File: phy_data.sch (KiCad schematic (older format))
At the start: 18 parts

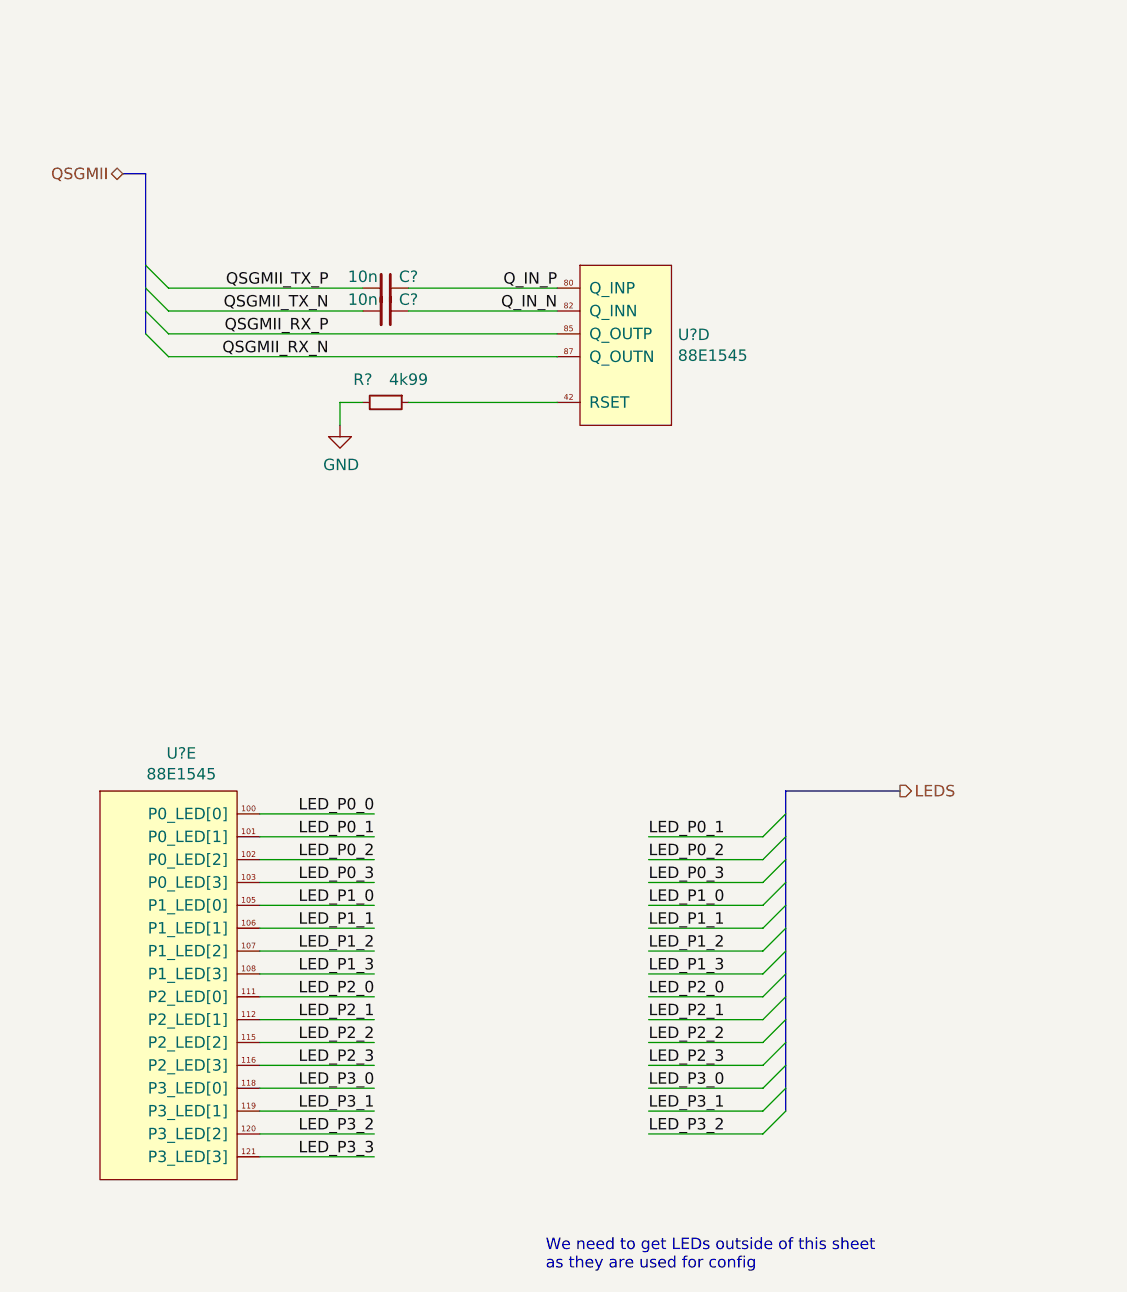
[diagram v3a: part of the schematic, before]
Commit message: sch: Remove ALL busses since kicad's support is broken
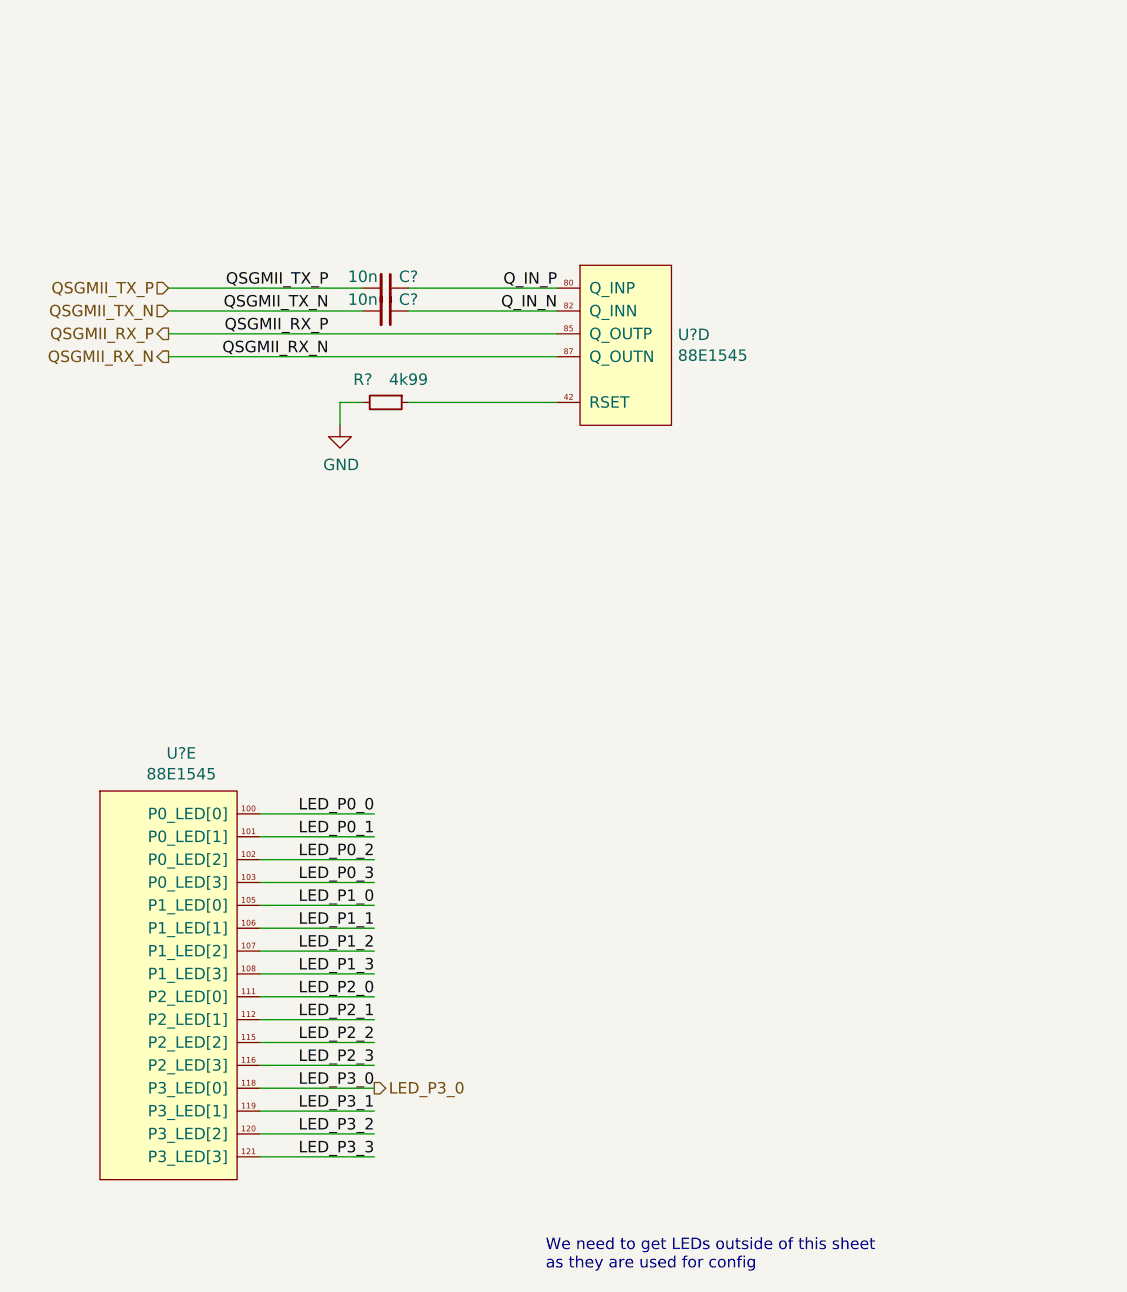
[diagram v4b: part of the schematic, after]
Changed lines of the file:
@@
 	1    0    0    -1
 $EndComp
-Text Label 3700 4600 0    50   ~ 0
-LED_P0_1
-Wire Wire Line
-	3700 4600 4200 4600
-Text Label 3700 4700 0    50   ~ 0
-LED_P0_2
-Wire Wire Line
-	3700 4700 4200 4700
-Text Label 3700 4800 0    50   ~ 0
-LED_P0_3
-Wire Wire Line
-	3700 4800 4200 4800
-Text Label 3700 4900 0    50   ~ 0
-LED_P1_0
-Wire Wire Line
-	3700 4900 4200 4900
-Text Label 3700 5000 0    50   ~ 0
-LED_P1_1
-Wire Wire Line
-	3700 5000 4200 5000
-Text Label 3700 5100 0    50   ~ 0
-LED_P1_2
-Wire Wire Line
-	3700 5100 4200 5100
-Text Label 3700 5200 0    50   ~ 0
-LED_P1_3
-Wire Wire Line
-	3700 5200 4200 5200
-Text Label 3700 5300 0    50   ~ 0
-LED_P2_0
-Wire Wire Line
-	3700 5300 4200 5300
-Text Label 3700 5400 0    50   ~ 0
-LED_P2_1
-Wire Wire Line
-	3700 5400 4200 5400
-Text Label 3700 5500 0    50   ~ 0
-LED_P2_2
-Wire Wire Line
-	3700 5500 4200 5500
-Text Label 3700 5600 0    50   ~ 0
-LED_P2_3
-Wire Wire Line
-	3700 5600 4200 5600
-Text Label 3700 5700 0    50   ~ 0
-LED_P3_0
-Wire Wire Line
-	3700 5700 4200 5700
-Text Label 3700 5800 0    50   ~ 0
-LED_P3_1
-Wire Wire Line
-	3700 5800 4200 5800
-Text Label 3700 5900 0    50   ~ 0
-LED_P3_2
-Wire Wire Line
-	3700 5900 4200 5900
-Wire Bus Line
-	4300 4400 4800 4400
-Entry Wire Line
-	4300 4500 4200 4600
-Entry Wire Line
-	4300 4600 4200 4700
-Entry Wire Line
-	4300 4700 4200 4800
-Entry Wire Line
-	4300 4800 4200 4900
-Entry Wire Line
-	4300 4900 4200 5000
-Entry Wire Line
-	4300 5000 4200 5100
-Entry Wire Line
-	4300 5100 4200 5200
-Entry Wire Line
-	4300 5200 4200 5300
-Entry Wire Line
-	4300 5300 4200 5400
-Entry Wire Line
-	4300 5400 4200 5500
-Entry Wire Line
-	4300 5500 4200 5600
-Entry Wire Line
-	4300 5600 4200 5700
-Entry Wire Line
-	4300 5700 4200 5800
-Entry Wire Line
-	4300 5800 4200 5900
-Text HLabel 4800 4400 2    50   Output ~ 0
-LEDS
-Wire Bus Line
-	1400 1700 1500 1700
-Text HLabel 1400 1700 0    50   BiDi ~ 0
-QSGMII
-Entry Wire Line
-	1500 2400 1600 2500
-Entry Wire Line
-	1500 2300 1600 2400
-Entry Wire Line
-	1500 2100 1600 2200
-Entry Wire Line
-	1500 2200 1600 2300
 Text Notes 3250 6500 0    50   ~ 0
 We need to get LEDs outside of this sheet\nas they are used for config
@@
 	0    1    1    0
 $EndComp
-Wire Bus Line
-	1500 1700 1500 2400
-Wire Bus Line
-	4300 4400 4300 5800
+Text HLabel 1600 2200 0    50   Input ~ 0
+QSGMII_TX_P
+Text HLabel 1600 2300 0    50   Input ~ 0
+QSGMII_TX_N
+Text HLabel 1600 2400 0    50   Output ~ 0
+QSGMII_RX_P
+Text HLabel 1600 2500 0    50   Output ~ 0
+QSGMII_RX_N
+Text HLabel 2500 5700 2    50   Output ~ 0
+LED_P3_0
 $EndSCHEMATC

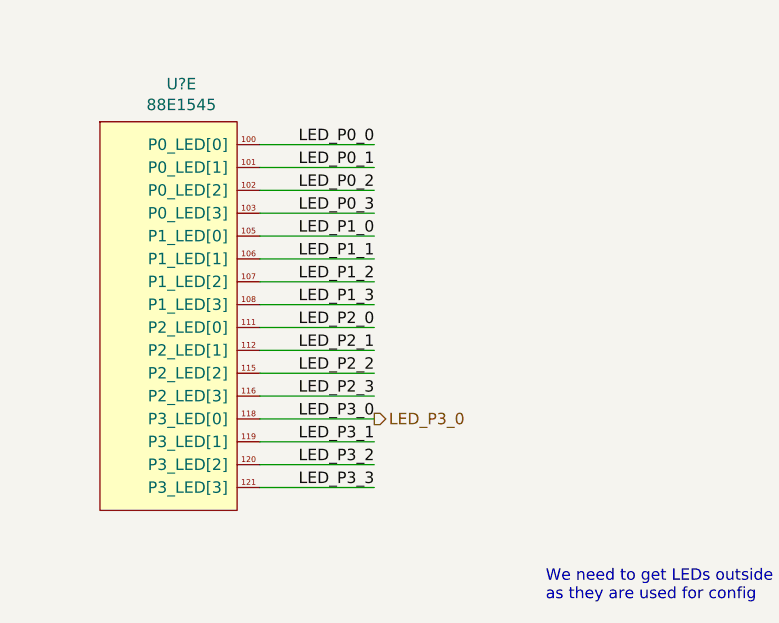
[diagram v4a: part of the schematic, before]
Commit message: lib, sch: Misc changes to make ERC happy
- add resistors to PCIe switch GPIOs
- add NC flags on PHY unused LED outputs
- add dummy supply on Earth PSU
- add dummy supply on PHY ref clock's VCC
- LTC3633: deduplicate SW1/2 outputs
- ILS8033: deduplicate LX1/2 and PGND1/2 outputs
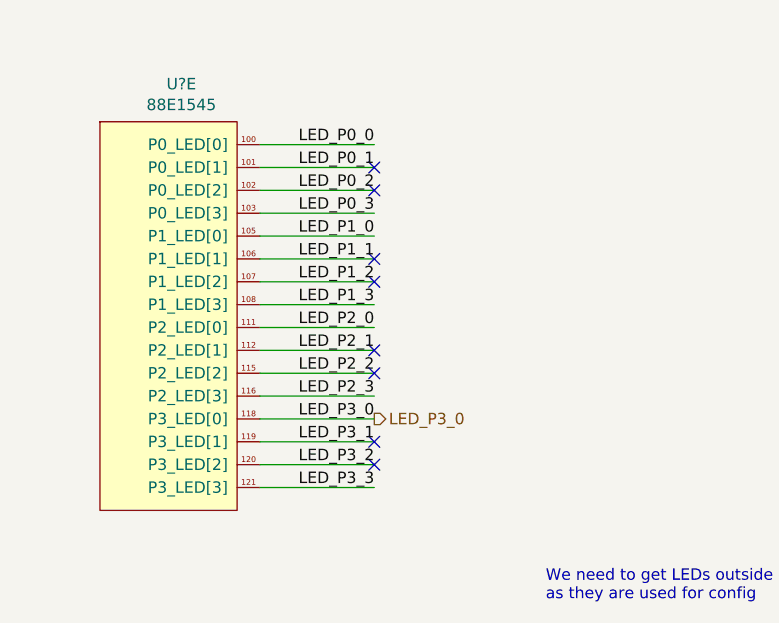
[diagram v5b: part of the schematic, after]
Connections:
- no-connect marks 0 -> 8
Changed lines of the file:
@@
 Text HLabel 2500 5700 2    50   Output ~ 0
 LED_P3_0
+NoConn ~ 2500 4600
+NoConn ~ 2500 4700
+NoConn ~ 2500 5000
+NoConn ~ 2500 5100
+NoConn ~ 2500 5400
+NoConn ~ 2500 5500
+NoConn ~ 2500 5800
+NoConn ~ 2500 5900
 $EndSCHEMATC
